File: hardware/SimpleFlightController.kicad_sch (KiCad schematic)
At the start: 7 parts, among them U1 BQ25887, U2 ICM-45686, U3 STM32F722RETx, U4 BMP580, U5 TPS63070RNMR

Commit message: stuff
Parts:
- removed U1: BQ25887, Package_DFN_QFN:VQFN-24-1EP_4x4mm_P0.5mm_EP2.5x2.5mm, symbol Battery_Management:BQ25887
- added R1, R2: 5.1K, symbol Device:R
- added U6: LMR51430, Package_TO_SOT_SMD:SOT-23-6, symbol Regulator_Switching:LMR51430
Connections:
- net GND: now reaches USB1.1 (GND)
- net GND: now also USB1.12 (GND), USB1.13 (SHELL), USB1.14 (SHELL), R1.2, R2.2
- net at USB1.10 (CC2): now also R2.1
- net VBUS: now reaches USB1.11 (VBUS)
- net VBUS: now also USB1.2 (VBUS)
- net at USB1.4 (CC1): now also R1.1
- net USB_DN: now reaches USB1.5 (DN2)
- net USB_DN: now also USB1.7 (DN1)
- net USB_DP: now reaches USB1.6 (DP1)
- net USB_DP: now also USB1.8 (DP2)
- no-connect marks 0 -> 2

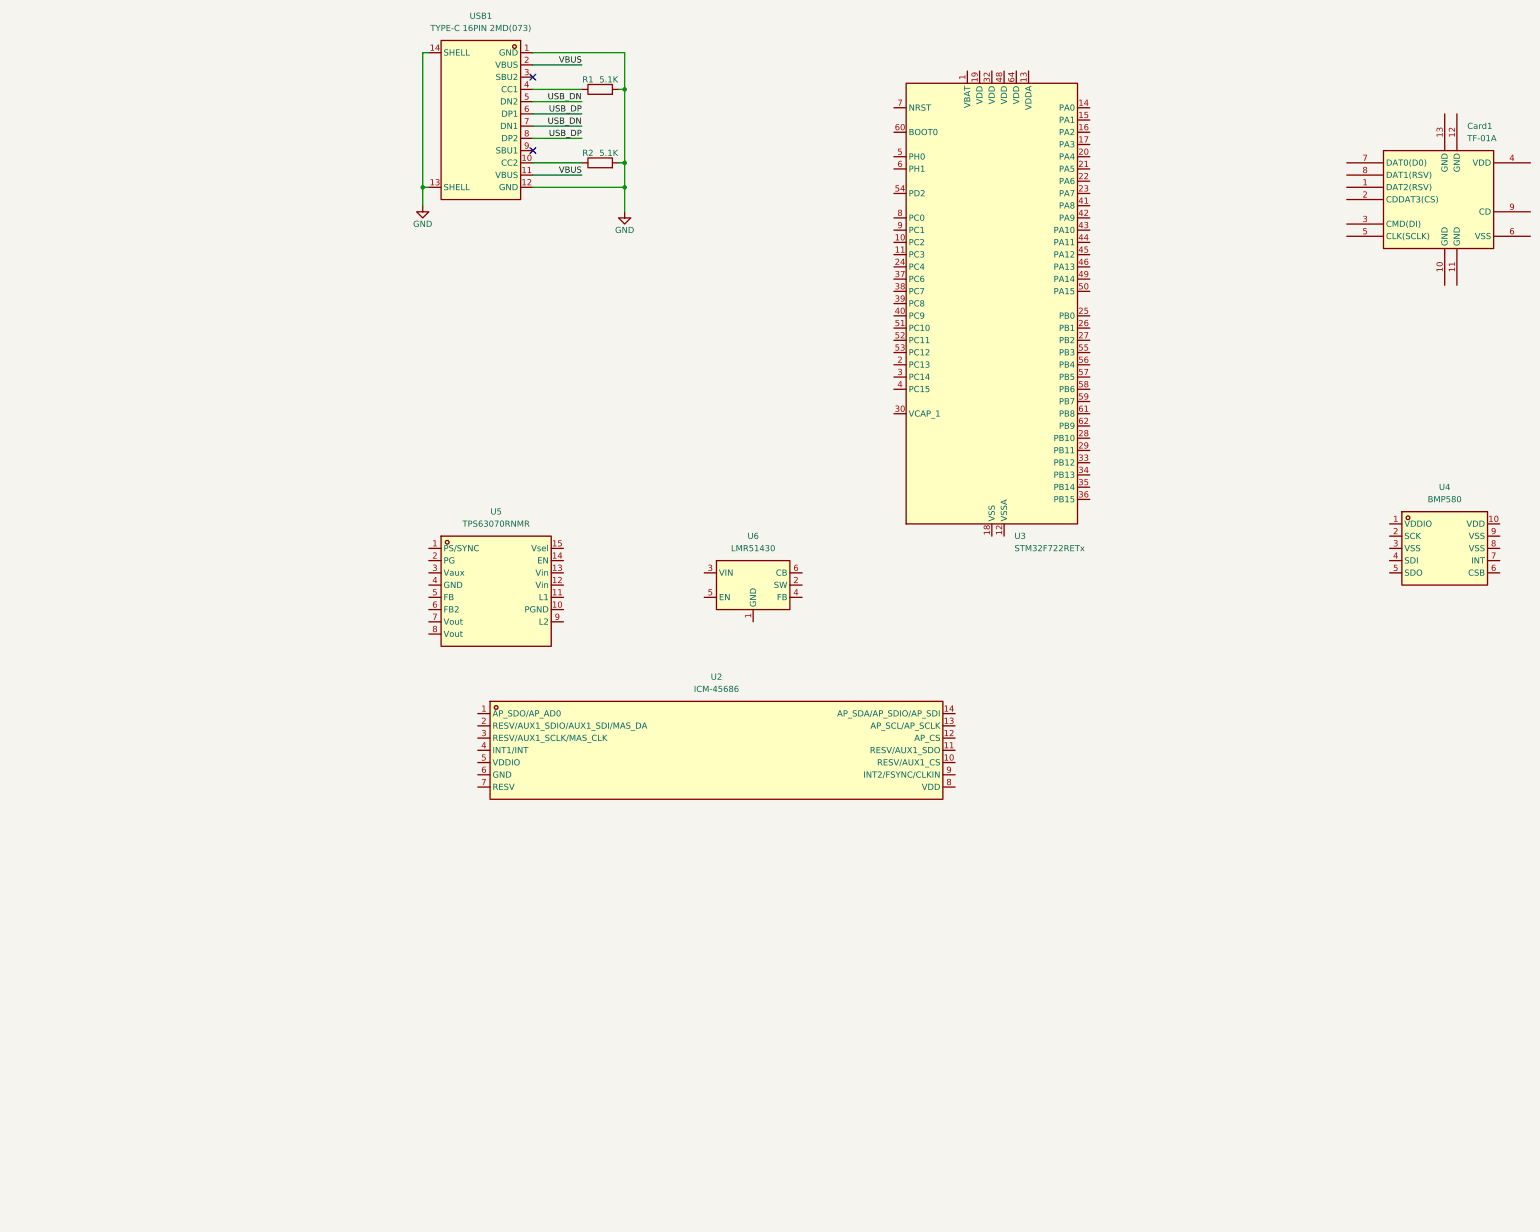
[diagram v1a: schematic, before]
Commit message: finished the 5v buck boost section
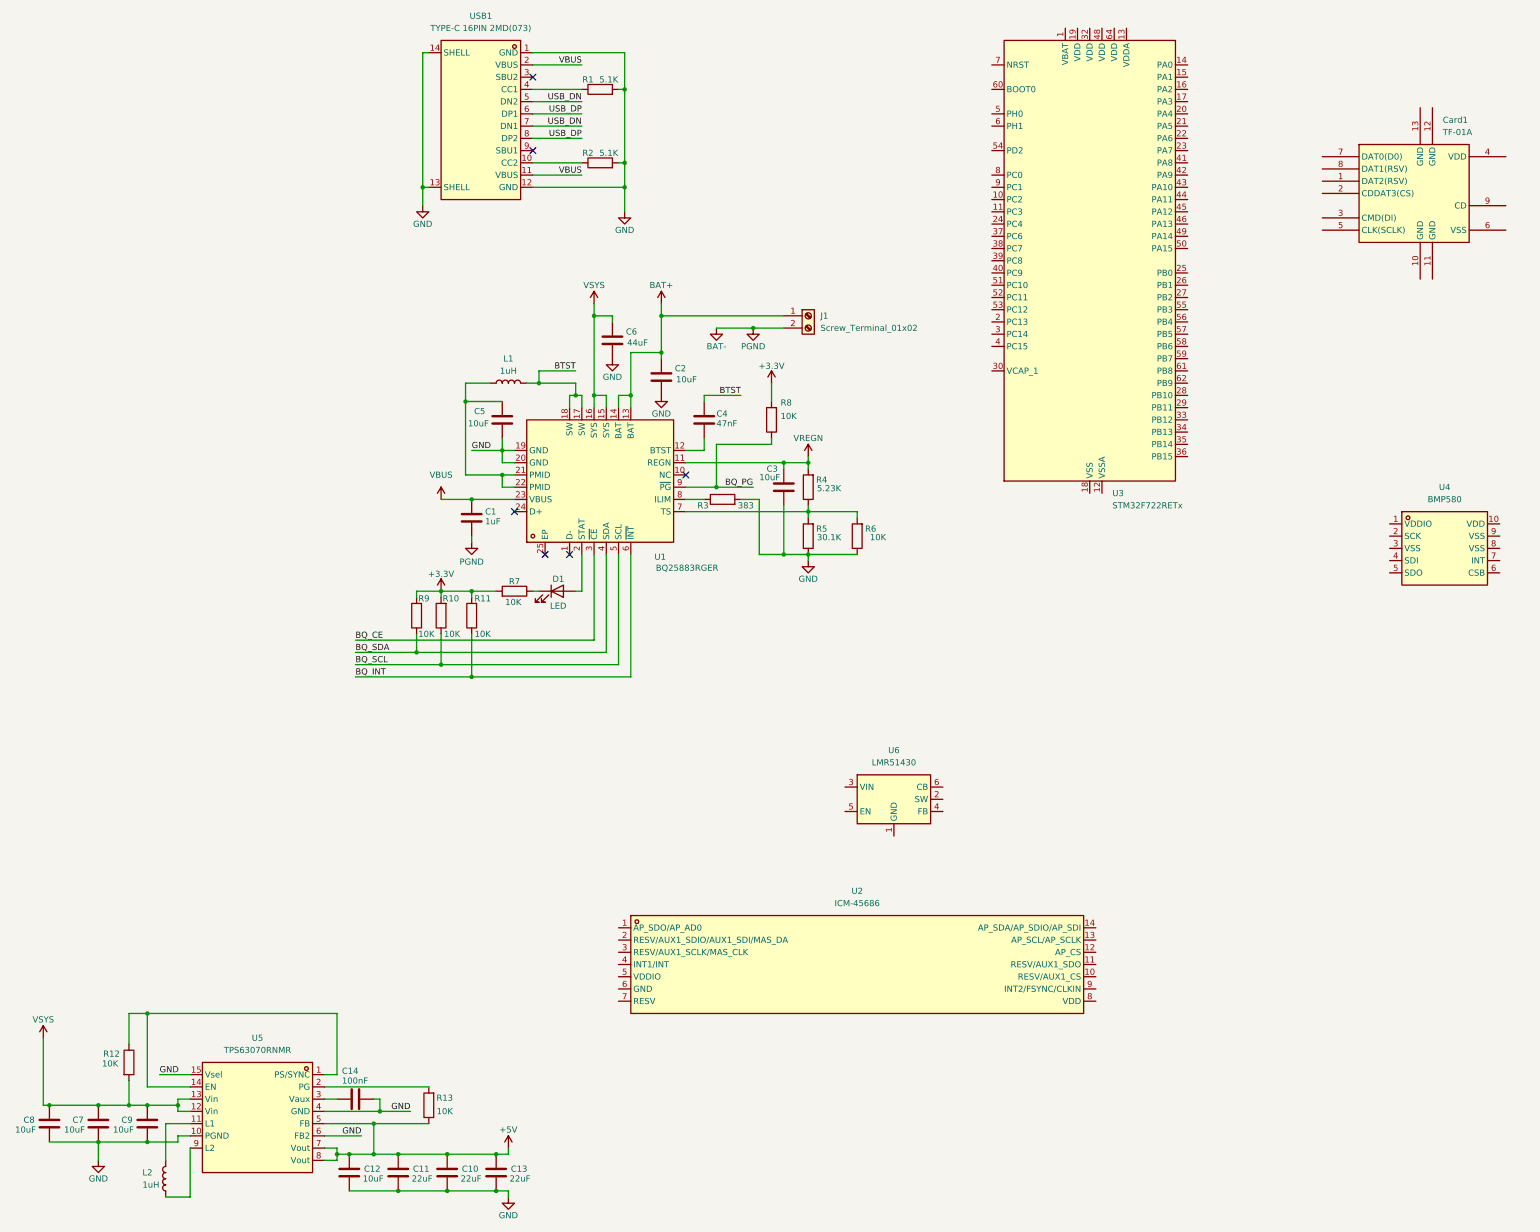
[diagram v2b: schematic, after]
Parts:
- added C1: 1uF, symbol Device:C
- added C10, C11, C13: 22uF, Capacitor_SMD:C_0805_2012Metric, symbol Device:C
- added C12, C9: 10uF, Capacitor_SMD:C_0603_1608Metric, symbol Device:C
- added C14: 100nF, symbol Device:C
- added C2, C3, C5: 10uF, symbol Device:C
- added C4: 47nF, symbol Device:C
- added C6: 44uF, symbol Device:C
- added C7, C8: 10uF, Capacitor_SMD:C_0805_2012Metric, symbol Device:C
- added D1: LED, symbol Device:LED
- added J1: Screw_Terminal_01x02, TerminalBlock:TerminalBlock_Xinya_XY308-2.54-2P_1x02_P2.54mm_Horizontal, symbol Connector:Screw_Terminal_01x02
- added L1, L2: 1uH, symbol Device:L
- added R10, R11, R12, R13, R6, R7, R8, R9: 10K, symbol Device:R
- added R3: 383, symbol Device:R
- added R4: 5.23K, symbol Device:R
- added R5: 30.1K, symbol Device:R
- added U1: BQ25883RGER, lcsc:VFQFPN-24_L4.0-W4.0-P0.50-BL-EP2.8, symbol lcsc:BQ25883RGER
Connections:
- net GND: now also U5.10 (PGND), U5.15 (Vsel), U5.4 (GND), U5.6 (FB2), C10.2, C11.2, C12.2, C13.2, C14.2, C2.2, C3.2, C5.2, C6.2, C7.2, C8.2, C9.2, R3.2, R5.1, R6.1, U1.19 (GND), U1.20 (GND)
- net VBUS: now also C1.1, U1.23 (VBUS)
- net at U5.1 (PS/SYNC): now also U5.14 (EN), R12.1
- net at U5.11 (L1): now also L2.2
- net VSYS: now reaches U5.12 (Vin)
- net VSYS: now also U5.13 (Vin), C6.1, C7.1, C8.1, C9.1, R12.2, U1.15 (SYS), U1.16 (SYS)
- net at U5.2 (PG): now also R13.2
- net at U5.3 (Vaux): now also C14.1
- net +5V: now reaches U5.5 (FB)
- net +5V: now also U5.7 (Vout), U5.8 (Vout), C10.1, C11.1, C12.1, C13.1, R13.1
- net at U5.9 (L2): now also L2.1
- new net: R4.1, R5.2, R6.2, U1.7 (TS)
- new net: R3.1, U1.8 (ILIM)
- new net: C5.1, L1.1, U1.21 (PMID), U1.22 (PMID)
- new net: D1.1 (K), R7.1
- new net: C4.2, U1.12 (BTST)
- new net: D1.2 (A), U1.2 (STAT)
- new net +3.3V: R10.2, R11.2, R7.2, R8.2, R9.2
- new net BAT+: C2.1, J1.1 (Pin_1), U1.13 (BAT), U1.14 (BAT)
- new net BAT-: C1.2, J1.2 (Pin_2)
- new net BQ_CE: U1.3 (~{CE})
- new net BQ_INT: R11.1, U1.6 (~{INT})
- new net BQ_PG: R8.1, U1.9 (~{PG})
- new net BQ_SCL: R10.1, U1.5 (SCL)
- new net BQ_SDA: R9.1, U1.4 (SDA)
- new net BTST: C4.1, L1.2, U1.17 (SW), U1.18 (SW)
- new net VREGN: C3.1, R4.2, U1.11 (REGN)
- no-connect marks 2 -> 6
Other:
- moved on the sheet: Card1, U2, U3, U5, U6

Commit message: added more stuff
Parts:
- added C15, C19, C20: 100nF, symbol Device:C
- added C16: 2.2uF, symbol Device:C
- added C17, C18: 22uF, symbol Device:C
- added L3: 5.6uH, symbol Device:L
- added R14: 100K, symbol Device:R
- added R15: 22.1K, symbol Device:R
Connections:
- net +3.3V: now also U4.1 (VDDIO), U4.10 (VDD), C17.1, C18.1, C19.1, C20.1, L3.2
- net GND: now also U4.3 (VSS), U4.5 (SDO), U4.6 (CSB), U4.8 (VSS), U4.9 (VSS), U6.1 (GND), C16.2, C17.2, C18.2, C19.2, C20.2, R15.1
- net VSYS: now also U6.3 (VIN), U6.5 (EN), C16.1
- net at U6.2 (SW): now also C15.2, L3.1, R14.2
- net at U6.4 (FB): now also R14.1, R15.2
- net at U6.6 (CB): now also C15.1
- net BMP_SCK: now reaches U4.2 (SCK)
- net BMP_SDI: now reaches U4.4 (SDI)
- net BMP_INT: now reaches U4.7 (INT)
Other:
- moved on the sheet: Card1, U2, U4, U6

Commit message: schematic done
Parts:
- added C21, C22, C23, C24, C25, C26, C27, C37: 100nF, symbol Device:C
- added C28, C29, C30: 1uF, symbol Device:C
- added C31: 10uF, symbol Device:C
- added C32: 2.2uF, symbol Device:C
- added C33, C34, C35, C36: 20pF, symbol Device:C
- added J2, J3: Conn_01x03, symbol Connector_Generic:Conn_01x03
- added L4: FCM1608KF-601T03, lcsc:L0603, symbol lcsc:FCM1608KF-601T03
- added R16, R17, R18, R19, R20, R21, R22: 10K, symbol Device:R
- added SW1, SW2: TS-1088-AR02016, lcsc:SW-SMD_L3.9-W3.0-P4.45, symbol lcsc:TS-1088-AR02016
- added X1: X322525MOB4SI, lcsc:CRYSTAL-SMD_4P-L3.2-W2.5-BL, symbol lcsc:X322525MOB4SI
- added X2: Q13FC1350000400, lcsc:FC-135R_L3.2-W1.5, symbol lcsc:Q13FC1350000400
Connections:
- net BMP_SCK is gone; now on net I2C_SCL: U4.2 (SCK)
- net BMP_SDI is gone; now on net I2C_SDA: U4.4 (SDI)
- net BQ_SCL is gone; now on net I2C_SCL: R10.1, U1.5 (SCL)
- net BQ_SDA is gone; now on net I2C_SDA: R9.1, U1.4 (SDA)
- net +3.3V: now also Card1.4 (VDD), U2.5 (VDDIO), U2.8 (VDD), U3.1 (VBAT), U3.19 (VDD), U3.32 (VDD), U3.48 (VDD), U3.64 (VDD), C21.1, C22.1, C23.1, C24.1, C25.1, C26.1, C27.1, C28.1, C29.1, C30.1, C31.1, L4.2, R16.2, R17.2, R18.2, R19.2, R20.2, R21.2, SW2.1
- net +5V: now also J2.1 (Pin_1), J3.1 (Pin_1)
- net BMP_INT: now also U3.62 (PB9)
- net BQ_CE: now also U3.61 (PB8)
- net BQ_INT: now also U3.57 (PB5)
- net GND: now also Card1.10 (GND), Card1.11 (GND), Card1.12 (GND), Card1.13 (GND), Card1.6 (VSS), U2.6 (GND), U3.12 (VSSA), U3.18 (VSS), U3.31 (VSS), U3.47 (VSS), U3.63 (VSS), C21.2, C22.2, C23.2, C24.2, C25.2, C26.2, C27.2, C28.2, C29.2, C30.2, C31.2, C32.2, C33.2, C34.2, C35.2, C36.2, C37.1, J2.3 (Pin_3), J3.3 (Pin_3), R22.1, SW1.1, X1.2 (GND), X1.4 (GND)
- net USB_DN: now also U3.44 (PA11)
- net USB_DP: now also U3.45 (PA12)
- net SD_DAT2: now reaches Card1.1 (DAT2(RSV))
- net SD_DAT2: now also U3.51 (PC10), R18.1
- net SD_DAT3: now reaches Card1.2 (CDDAT3(CS))
- net SD_DAT3: now also U3.52 (PC11), R19.1
- net SD_CMD: now reaches Card1.3 (CMD(DI))
- net SD_CMD: now also U3.54 (PD2), R20.1
- net SD_CLK: now reaches Card1.5 (CLK(SCLK))
- net SD_CLK: now also U3.53 (PC12), R21.1
- net SD_DAT0: now reaches Card1.7 (DAT0(D0))
- net SD_DAT0: now also U3.39 (PC8), R16.1
- net SD_DAT1: now reaches Card1.8 (DAT1(RSV))
- net SD_DAT1: now also U3.40 (PC9), R17.1
- net SD_CD: now reaches Card1.9 (CD)
- net SD_CD: now also U3.55 (PB3)
- net at U3.13 (VDDA): now also L4.1
- net SERVO1: now reaches U3.14 (PA0)
- net SERVO1: now also J2.2 (Pin_2)
- net SERVO2: now reaches U3.15 (PA1)
- net SERVO2: now also J3.2 (Pin_2)
- net ICM_CS: now reaches U3.20 (PA4)
- net ICM_CS: now also U2.12 (AP_CS)
- net ICM_SCK: now reaches U3.21 (PA5)
- net ICM_SCK: now also U2.13 (AP_SCL/AP_SCLK)
- net ICM_SDO: now reaches U3.22 (PA6)
- net ICM_SDO: now also U2.1 (AP_SDO/AP_AD0)
- net ICM_SDI: now reaches U3.23 (PA7)
- net ICM_SDI: now also U2.14 (AP_SDA/AP_SDIO/AP_SDI)
- net ICM_INT1: now reaches U3.24 (PC4)
- net ICM_INT1: now also U2.4 (INT1/INT), U3.41 (PA8)
- net ICM_INT2: now reaches U3.25 (PB0)
- net ICM_INT2: now also U2.9 (INT2/FSYNC/CLKIN), U3.42 (PA9)
- net LSE_IN: now reaches U3.3 (PC14)
- net LSE_IN: now also C35.1, X2.1
- net at U3.30 (VCAP_1): now also C32.1
- net LSE_OUT: now reaches U3.4 (PC15)
- net LSE_OUT: now also C36.1, X2.2
- net HSE_IN: now reaches U3.5 (PH0)
- net HSE_IN: now also C33.1, X1.1 (OSC1)
- net I2C_SCL: now reaches U3.58 (PB6)
- net I2C_SDA: now reaches U3.59 (PB7)
- net HSE_OUT: now reaches U3.6 (PH1)
- net HSE_OUT: now also C34.1, X1.3 (OSC2)
- net BOOT: now reaches U3.60 (BOOT0)
- net BOOT: now also R22.2, SW2.2
- net RESET: now reaches U3.7 (NRST)
- net RESET: now also C37.2, SW1.2
- net BAT- renamed PGND
- no-connect marks 6 -> 33
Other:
- note added: "3.3V Buck"
- note added: "5V Buck-Boost"
- note added: "Battery Charger"
- note added: "Buttons"
- note added: "Crystals"
- note added: "Decoupling"
- note added: "IMU"
- note added: "Pressure Sensor"
- note added: "STM32"
- note added: "Servos"
- note added: "Simple Flight Controller"
- note added: "USB-C"
- note added: "microSD Card"
- moved on the sheet: C1, C10, C11, C12, C13, C14, C15, C16, C17, C18, C19, C2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

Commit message: finish guide and board
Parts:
- removed L1, L2: 1uH, symbol Device:L
- removed L3: 5.6uH, symbol Device:L
- added L5: DFE252012F-1R0M=P2, lcsc:L2520, symbol lcsc:DFE252012F-1R0M=P2
- added L6: XFL4020-152MEC, lcsc:IND-SMD_L4.0-W4.0-A, symbol lcsc:XFL4020-152MEC
- added L7: YHNR3015-5R6M, lcsc:IND-SMD_L3.0-W3.0, symbol lcsc:YHNR3015-5R6M
- C1, C17, C18, C28, C29, C3, C30, C31, C5: footprint (none) -> Capacitor_SMD:C_0402_1005Metric
- C14, C15, C19, C20, C21, C22, C23, C24, C25, C26, C27, C32, C33, C34, C35, C36, C37, C4: footprint (none) -> Capacitor_SMD:C_0201_0603Metric
- C16, C2, C6: footprint (none) -> Capacitor_SMD:C_0603_1608Metric
- D1: footprint (none) -> LED_SMD:LED_0402_1005Metric
- J2, J3: footprint (none) -> Connector_PinHeader_2.54mm:PinHeader_1x03_P2.54mm_Vertical
- R1, R10, R11, R12, R13, R16, R17, R18, R19, R2, R20, R21, R22, R3, R4, R5, R6, R7, R8, R9: footprint (none) -> Resistor_SMD:R_0201_0603Metric
- R14, R15: footprint (none) -> Resistor_SMD:R_0402_1005Metric
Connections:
- net PGND is gone; now on net GND: C1.2, J1.2 (Pin_2)
- net +3.3V: now also L7.2
- net BTST: now also L5.1
- net GND: now also U1.25 (EP)
- net ICM_INT1: no longer U3.41 (PA8)
- net ICM_INT2: no longer U3.42 (PA9)
- net at U5.9 (L2): now also L6.1
- net at U5.11 (L1): now also L6.2
- net at C15.2, R14.2, U6.2 (SW): now also L7.1
- net at C5.1, U1.21 (PMID), U1.22 (PMID): now also L5.2
- no-connect marks 33 -> 34

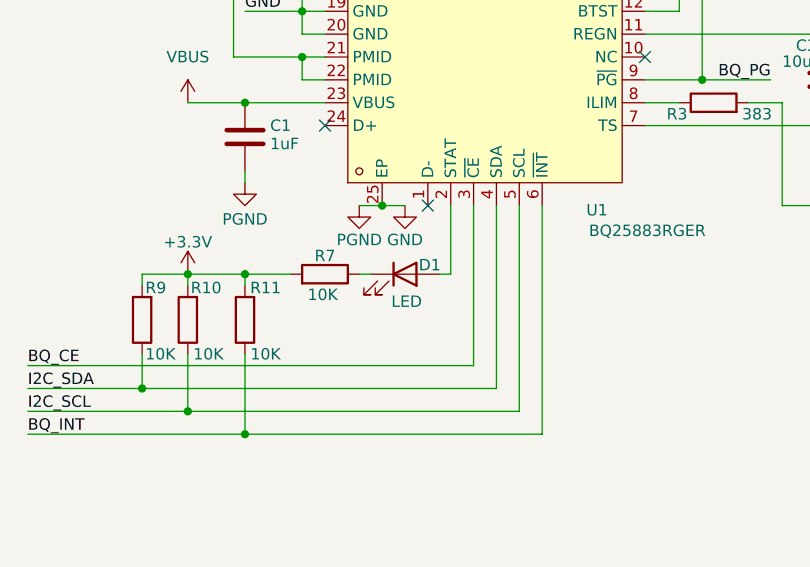
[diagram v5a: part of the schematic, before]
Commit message: flip led
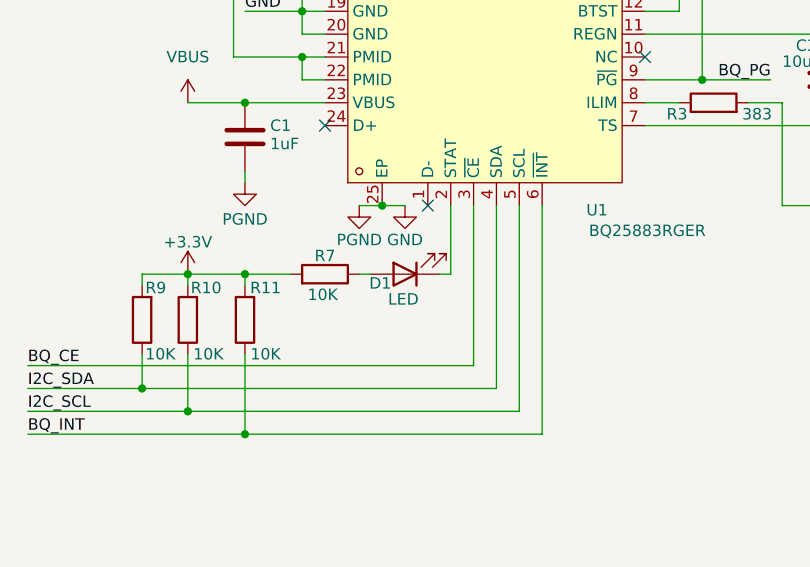
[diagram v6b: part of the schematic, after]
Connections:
- net at R7.1: now also D1.2 (A); no longer D1.1 (K)
- net at U1.2 (STAT): now also D1.1 (K); no longer D1.2 (A)
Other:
- moved on the sheet: D1
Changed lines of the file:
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@@
 	(symbol
 		(lib_id "Device:LED")
-		(at 67.31 175.26 0)
+		(at 67.31 175.26 180)
 		(unit 1)
 		(exclude_from_sim no)
@@
 		(dnp no)
 		(property "Reference" "D1"
-			(at 68.834 174.244 0)
+			(at 65.786 176.276 0)
 			(effects
 				(font
@@
 		)
 		(property "Value" "LED"
-			(at 65.786 178.308 0)
+			(at 68.834 178.054 0)
 			(effects
 				(font

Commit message: guide
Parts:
- C35, C36: value 20pF -> 6.8pF
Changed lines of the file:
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@@
 			)
 		)
-		(property "Value" "20pF"
-			(at 161.544 72.39 0)
+		(property "Value" "6.8pF"
+			(at 162.306 72.39 0)
 			(effects
 				(font
@@
 			)
 		)
-		(property "Value" "20pF"
-			(at 135.636 72.39 0)
-			(effects
-				(font
+		(property "Value" "6.8pF"
+			(at 135.128 72.39 0)
+			(effects
+				(font
